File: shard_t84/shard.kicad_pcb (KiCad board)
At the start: 2 copper layers, 35 x 31 mm, 8 parts, among them J0 Shard, J1 ISP, U1 ATtiny84

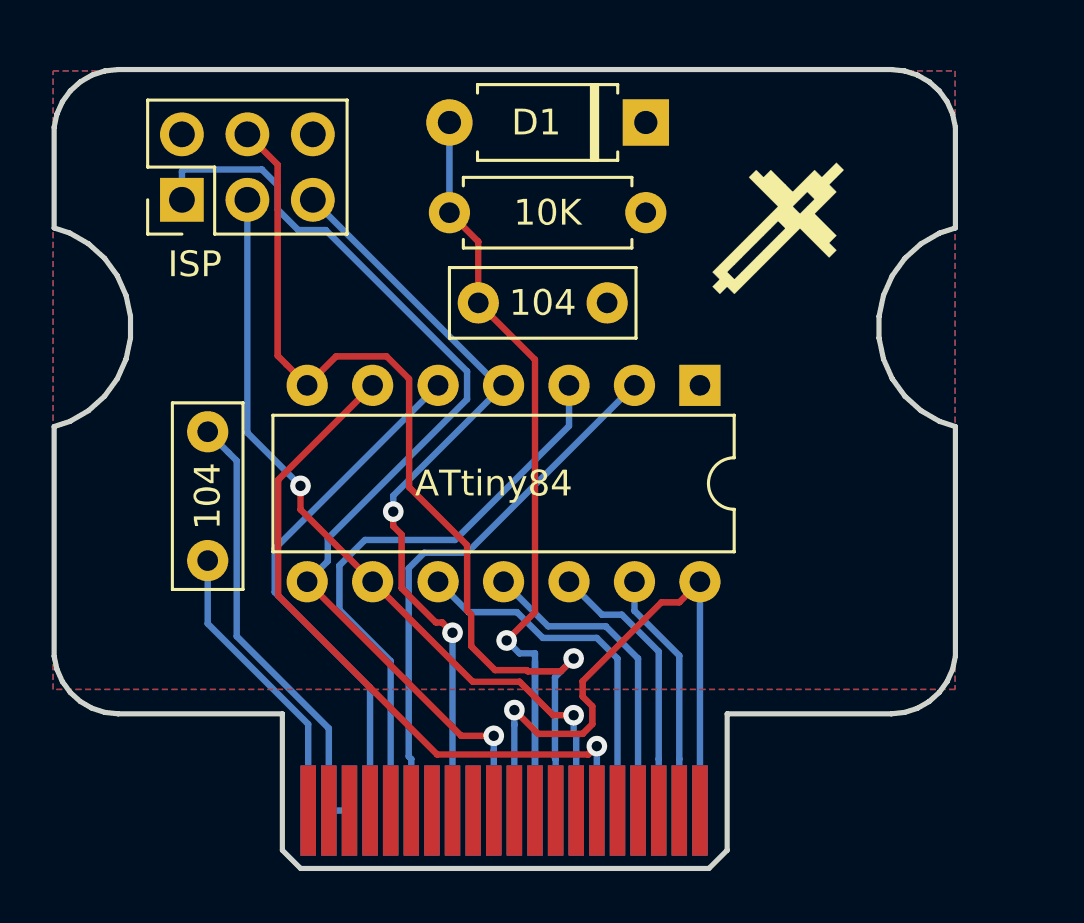
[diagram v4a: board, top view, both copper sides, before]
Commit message: fixed issues with shard
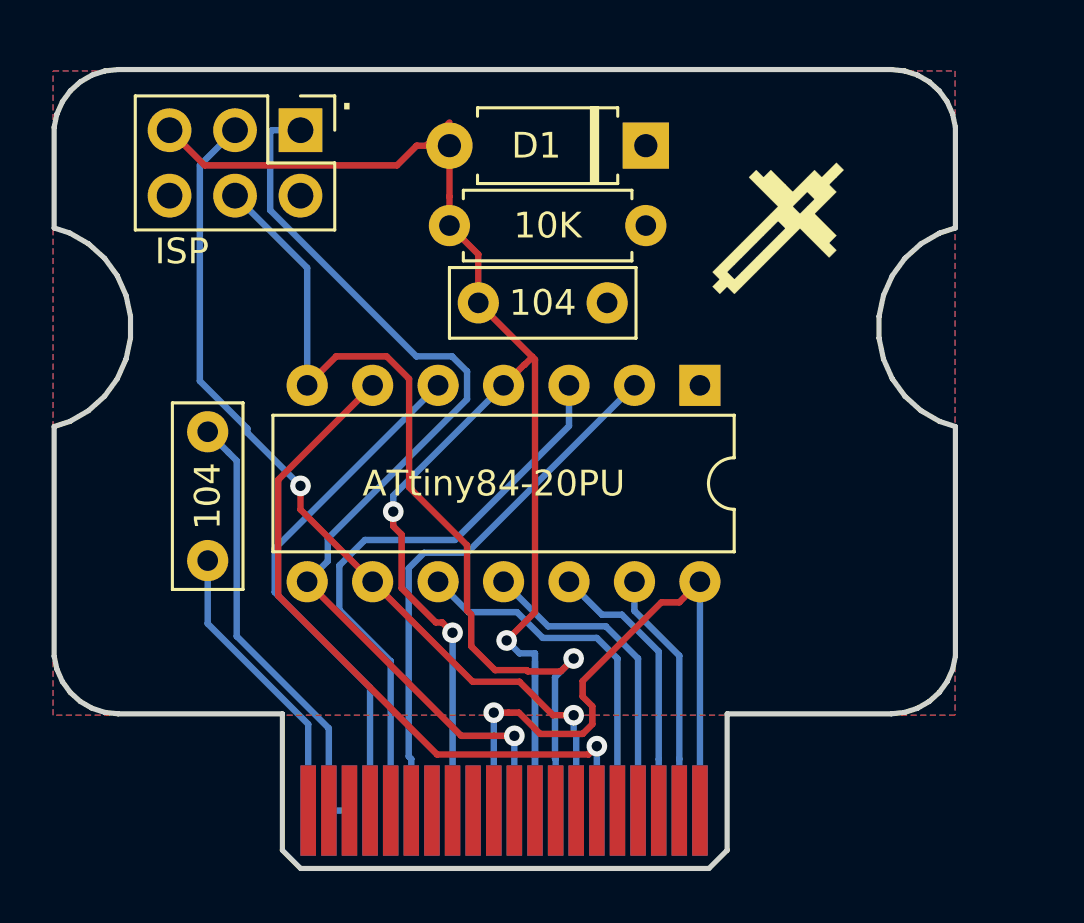
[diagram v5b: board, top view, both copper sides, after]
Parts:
- U1: value ATtiny84 -> ATtiny84-20PU
- moved J1 5.33 mm to (126.6, 53.3), turned to 270 degrees
- moved D1 0.90 mm to (140.0, 53.9)
- moved R1 0.50 mm to (140.0, 57.0)
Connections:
- J0 pad 1: Net-(J0-Pad1) -> (no net)
- J0 pad 11: Net-(J0-Pad11) -> (no net)
- J0 pad 13: Net-(J0-Pad13) -> (no net)
- J0 pad 14: Net-(J0-Pad14) -> (no net)
- J0 pad 15: Net-(J0-Pad15) -> (no net)
- J0 pad 16: RESET -> D_RST
- J0 pad 17: Net-(J0-Pad17) -> (no net)
- J0 pad 18: Net-(J0-Pad18) -> (no net)
- J0 pad 19: Net-(J0-Pad19) -> (no net)
- J0 pad 20: D_DC -> GND
- J0 pad 21: Net-(J0-Pad21) -> (no net)
- J0 pad 22: GND -> D_DC
- J0 pad 23: Net-(J0-Pad23) -> (no net)
- J0 pad 25: Net-(J0-Pad25) -> (no net)
- J0 pad 27: Net-(J0-Pad27) -> (no net)
- J0 pad 29: Net-(J0-Pad29) -> (no net)
- J0 pad 3: Net-(J0-Pad3) -> (no net)
- J0 pad 31: Net-(J0-Pad31) -> (no net)
- J0 pad 33: Net-(J0-Pad33) -> (no net)
- J0 pad 35: Net-(J0-Pad35) -> (no net)
- J0 pad 37: Net-(J0-Pad37) -> (no net)
- J0 pad 39: Net-(J0-Pad39) -> (no net)
- J0 pad 5: Net-(J0-Pad5) -> (no net)
- J0 pad 7: Net-(J0-Pad7) -> (no net)
- J0 pad 9: Net-(J0-Pad9) -> (no net)
- J1 pad 5: RESET -> D_RST
- U1 pad 4: RESET -> D_RST
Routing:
- net D_RST: track 35.1 -> 68.4 mm, vias 1 -> 3
- net RESET: track 29.8 -> 0.00 mm, vias 2 -> 0
- net D_SCK: track 30.5 -> 34.5 mm
- net D_MOSI: track 37.7 -> 35.5 mm
- net D_DC: track 39.3 -> 38.6 mm
- net GND: track 41.8 -> 42.4 mm
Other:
- board text added: "."
